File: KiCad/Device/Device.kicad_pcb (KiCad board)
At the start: 2 copper layers, 27 parts, among them IC1 ATTINY167-XUR, J1 Mikrofon, J2 Lysføler, J3 Optisk sensor, J4 Fugtføler, J5 VCC, J6 ESP8266(wifi), SW1 SW_MEC_5E, SW3 SW_MEC_5E, SW4 SW_DIP_x02, Y1 Crystal

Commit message: Fungerende_men_grimt_print
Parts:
- D3: footprint Diode_SMD:D_MELF_Handsoldering -> Resistor_THT:R_Axial_DIN0309_L9.0mm_D3.2mm_P12.70mm_Horizontal
- moved SW3 54.1 mm to (182.2, 61.2)
- moved R6 51.0 mm to (169.3, 93.0), turned to 180 degrees
- moved SW1 46.1 mm to (166.9, 61.1)
- moved D3 44.4 mm to (124.5, 71.1)
- moved C4 43.8 mm to (174.9, 78.0)
- moved D1 40.8 mm to (147.3, 61.0)
- moved J6 39.2 mm to (162.6, 76.2)
- moved D2 36.0 mm to (154.9, 61.0)
- moved C2 35.1 mm to (154.9, 111.8), turned to -90 degrees
- moved R5 34.8 mm to (165.2, 69.0), turned to 180 degrees
- moved Y1 30.9 mm to (162.6, 106.7), turned to -90 degrees
- moved J5 29.7 mm to (121.9, 63.5)
- moved C1 25.4 mm to (195.6, 91.4), turned to -90 degrees
- moved C3 24.3 mm to (170.2, 111.7), turned to -90 degrees
- moved R1 23.2 mm to (132.7, 101.0)
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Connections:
- SW1 pad 2: unconnected-(SW1-Pad2) -> Button01
- SW3 pad 2: unconnected-(SW3-Pad2) -> Reset
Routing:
- net +5V: track 0.00 -> 239.5 mm
- net Reset: track 0.00 -> 134.1 mm, vias 0 -> 4
- net Photo_out: track 0.00 -> 121.2 mm, vias 0 -> 4
- net Net-(C1-Pad1): track 0.00 -> 120.9 mm, vias 0 -> 2
- net Op.Sensor_out: track 0.00 -> 118.6 mm, vias 0 -> 2
- net Fugt_out: track 0.00 -> 105.8 mm
- net Button01: track 0.00 -> 100.3 mm
- net +3,3V: track 0.00 -> 95.5 mm, vias 0 -> 3
- net Net-(D1-Pad1): track 0.00 -> 71.3 mm
- net SCL: track 0.00 -> 50.8 mm, vias 0 -> 2
- net GrønLED: track 0.00 -> 50.3 mm, vias 0 -> 2
- net Net-(D2-Pad1): track 0.00 -> 41.8 mm, vias 0 -> 2
- net SDA: track 0.00 -> 35.3 mm, vias 0 -> 2
- net XTAL1: track 0.00 -> 28.9 mm
- net XTAL2: track 0.00 -> 17.1 mm
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- added copper zone on B.Cu, net GND
- added copper zone on F.Cu, net GND
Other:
- board outline added: 109.6 x 72.2 mm
- board text added: "0 V"
- board text added: "Fugtføler"
- board text added: "Lysføler"
- board text added: "Mic"
- board text added: "Opt. sen."
- board text added: "PAIR"
- board text added: "RESET"
- board text added: "VCC"

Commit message: save
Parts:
- removed J1: Mikrofon, Connector_Phoenix_MC_HighVoltage:PhoenixContact_MCV_1,5_2-G-5.08_1x02_P5.08mm_Vertical
- removed J2: Lysføler, Connector_PinSocket_2.54mm:PinSocket_2x01_P2.54mm_Vertical
- removed J3: Optisk sensor, Connector_PinSocket_2.54mm:PinSocket_2x02_P2.54mm_Vertical
- removed J4: Fugtføler, Connector_PinSocket_2.54mm:PinSocket_1x03_P2.54mm_Vertical
- removed R3: 10k, Resistor_THT:R_Axial_DIN0309_L9.0mm_D3.2mm_P12.70mm_Horizontal
- added J7: Conn_02x06_Counter_Clockwise, Connector_PinHeader_2.54mm:PinHeader_2x06_P2.54mm_Horizontal, F.Cu at (77.1, 35.8)
- added R10: 15, Resistor_THT:R_Axial_DIN0309_L9.0mm_D3.2mm_P12.70mm_Horizontal, F.Cu at (62.8, 69.4)
- C4: footprint Capacitor_THT:C_Disc_D5.0mm_W2.5mm_P5.00mm -> Capacitor_THT:CP_Axial_L10.0mm_D4.5mm_P15.00mm_Horizontal
- D3: footprint Resistor_THT:R_Axial_DIN0309_L9.0mm_D3.2mm_P12.70mm_Horizontal -> Diode_THT:D_DO-15_P10.16mm_Horizontal
- moved C3 138.1 mm to (44.2, 54.9)
- moved C1 133.3 mm to (65.5, 62.1), turned to 0 degrees
- moved IC1 131.7 mm to (60.1, 36.1)
- moved Y1 126.3 mm to (49.6, 50.1)
- moved C2 125.5 mm to (44.4, 52.3), turned to 90 degrees
- moved J6 124.9 mm to (44.2, 36.3)
- moved R6 123.5 mm to (56.6, 42.7), turned to 90 degrees
- moved C4 116.9 mm to (58.9, 63.6), turned to 180 degrees
- moved D1 111.8 mm to (36.3, 74.2), turned to 90 degrees
- moved R5 110.4 mm to (55.2, 59.1), turned to 90 degrees
- moved SW3 107.7 mm to (75.5, 76.1)
- moved SW4 91.7 mm to (46.2, 86.3)
- moved J5 85.8 mm to (38.8, 84.8), turned to 90 degrees
- moved SW1 85.0 mm to (82.0, 61.1), turned to 180 degrees
- moved R4 83.2 mm to (78.5, 29.8), turned to 180 degrees
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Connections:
- net GrønLED renamed LED_G
- net Net-(C1-Pad1) renamed MIC
- C1 pad 2: Mic_out -> UP7
- C4 pad 1: +3,3V -> +3V3
- D3 pad 1: +3,3V -> +3V3
- IC1 pad 11: unconnected-(IC1-Pad11) -> UP7
- IC1 pad 12: unconnected-(IC1-Pad12) -> PHOTRAN
- IC1 pad 13: Op.Sensor_out -> UP5
- IC1 pad 14: Fugt_out -> UP4
- IC1 pad 17: Photo_out -> OPTISK
- IC1 pad 18: Mic_out -> UP2
- IC1 pad 19: unconnected-(IC1-Pad19) -> UP1
- IC1 pad 20: unconnected-(IC1-Pad20) -> DHT11
- J6 pad 4: +3,3V -> +3V3
- J6 pad 8: +3,3V -> +3V3
- R1 pad 1: Photo_out -> PHOTRAN
- R4 pad 1: Op.Sensor_out -> OPTISK
- R9 pad 1: +5V -> +3V3
- R9 pad 2: +3,3V -> +5V
- SW4 pad 2: unconnected-(SW4-Pad2) -> UPWR
- SW4 pad 3: unconnected-(SW4-Pad3) -> +3V3
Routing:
- net Photo_out: track 121.2 -> 0.00 mm, vias 4 -> 0
- net Op.Sensor_out: track 118.6 -> 0.00 mm, vias 2 -> 0
- net MIC: track 120.9 -> 11.6 mm, vias 2 -> 0
- net Fugt_out: track 105.8 -> 0.00 mm
- net +3,3V: track 95.5 -> 0.00 mm, vias 3 -> 0
- net +3V3: track 0.00 -> 75.4 mm
- net Net-(D1-Pad1): track 71.3 -> 4.49 mm
- net Reset: track 134.1 -> 75.2 mm, vias 4 -> 0
- net UP5: track 0.00 -> 57.1 mm
- net UPWR: track 0.00 -> 57.0 mm
- net Button01: track 100.3 -> 53.5 mm
- net OPTISK: track 0.00 -> 45.0 mm
- net +5V: track 239.5 -> 200.4 mm
- net GND: track 0.00 -> 31.7 mm
- net UP7: track 0.00 -> 31.6 mm
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- removed copper zone on B.Cu, net GND
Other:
- board size 109.6 x 72.2 mm -> 53.5 x 62.2 mm
- board text removed: "0 V"
- board text removed: "Fugtføler"
- board text removed: "Lysføler"
- board text removed: "Mic"
- board text removed: "Opt. sen."
- board text removed: "PAIR"
- board text removed: "RESET"
- board text removed: "VCC"

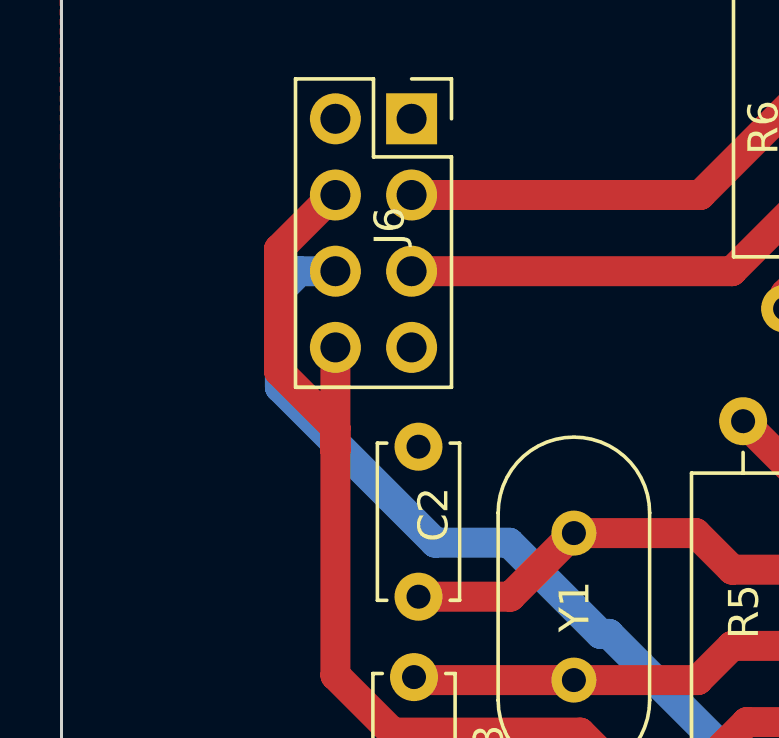
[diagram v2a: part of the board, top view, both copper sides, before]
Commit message: Ny_connecter
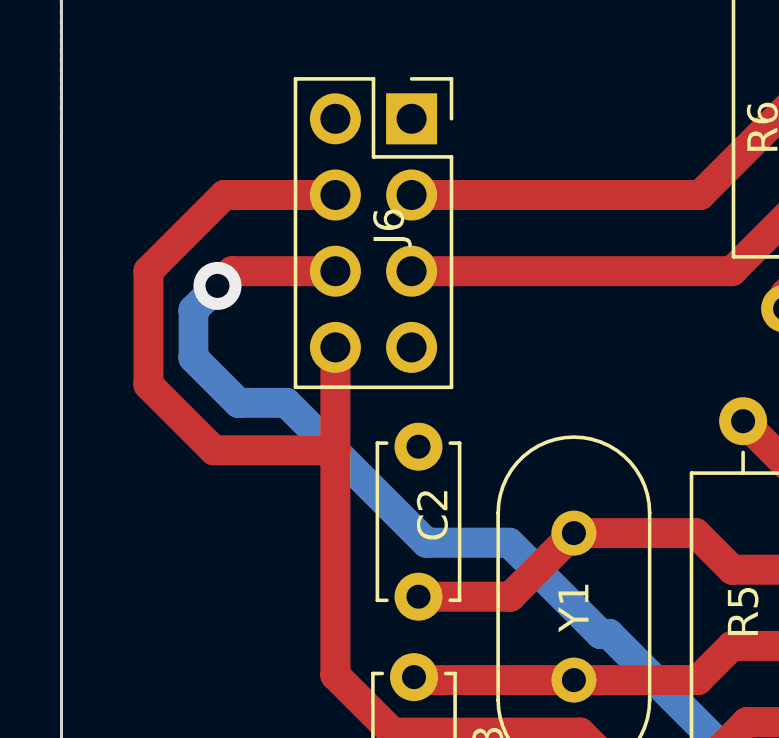
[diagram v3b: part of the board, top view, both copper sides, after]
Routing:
- net +3V3: track 75.4 -> 83.5 mm
- net Reset: track 75.2 -> 80.0 mm, vias 0 -> 1
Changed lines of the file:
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@@
   (segment (start 41.63 54.88) (end 43.539511 56.789511) (width 1) (layer "F.Cu") (net 6))
   (segment (start 49.789511 56.789511) (end 51.410489 58.410489) (width 1) (layer "F.Cu") (net 6))
-  (segment (start 39.75 44.74) (end 39.75 42) (width 1) (layer "F.Cu") (net 6))
+  (segment (start 35.4 45.2) (end 35.4 41.4) (width 1) (layer "F.Cu") (net 6))
   (segment (start 58.86 69.48) (end 58.91 69.43) (width 1) (layer "F.Cu") (net 6))
-  (segment (start 41.554395 38.87) (end 39.75 40.674395) (width 1) (layer "F.Cu") (net 6))
   (segment (start 51.410489 77.910489) (end 52.175 78.675) (width 1) (layer "F.Cu") (net 6))
+  (segment (start 41.63 47.38) (end 37.58 47.38) (width 1) (layer "F.Cu") (net 6))
   (segment (start 41.63 43.95) (end 41.63 47.38) (width 1) (layer "F.Cu") (net 6))
   (segment (start 54.295 78.675) (end 58.86 74.11) (width 1) (layer "F.Cu") (net 6))
   (segment (start 52.175 78.675) (end 54.295 78.675) (width 1) (layer "F.Cu") (net 6))
+  (segment (start 37.58 47.38) (end 35.4 45.2) (width 1) (layer "F.Cu") (net 6))
   (segment (start 48.74 78.675) (end 52.175 78.675) (width 1) (layer "F.Cu") (net 6))
-  (segment (start 41.63 38.87) (end 41.554395 38.87) (width 1) (layer "F.Cu") (net 6))
+  (segment (start 35.4 41.4) (end 37.93 38.87) (width 1) (layer "F.Cu") (net 6))
   (segment (start 58.86 64.445) (end 58.91 64.395) (width 1) (layer "F.Cu") (net 6))
-  (segment (start 39.75 44.74) (end 41.63 46.62) (width 1) (layer "F.Cu") (net 6))
   (segment (start 41.63 47.38) (end 41.63 54.88) (width 1) (layer "F.Cu") (net 6))
-  (segment (start 41.63 46.62) (end 41.63 47.38) (width 1) (layer "F.Cu") (net 6))
-  (segment (start 39.75 40.674395) (end 39.75 42) (width 1) (layer "F.Cu") (net 6))
   (segment (start 51.410489 58.410489) (end 51.410489 77.910489) (width 1) (layer "F.Cu") (net 6))
   (segment (start 43.539511 56.789511) (end 49.789511 56.789511) (width 1) (layer "F.Cu") (net 6))
+  (segment (start 37.93 38.87) (end 41.63 38.87) (width 1) (layer "F.Cu") (net 6))
   (segment (start 58.86 73.5) (end 58.86 64.445) (width 1) (layer "F.Cu") (net 6))
   (segment (start 58.86 74.11) (end 58.86 72.75) (width 1) (layer "F.Cu") (net 6))
@@
   (segment (start 53.21 76.63) (end 53.21 58.575106) (width 1) (layer "F.Cu") (net 14))
   (segment (start 55.345106 56.44) (end 60.14 56.44) (width 1) (layer "F.Cu") (net 14))
+  (segment (start 38.19 41.41) (end 41.63 41.41) (width 1) (layer "F.Cu") (net 15))
   (segment (start 55.22 59.11) (end 60.01 59.11) (width 1) (layer "F.Cu") (net 15))
   (segment (start 60.01 59.11) (end 60.14 58.98) (width 1) (layer "F.Cu") (net 15))
+  (segment (start 37.7 41.9) (end 38.19 41.41) (width 1) (layer "F.Cu") (net 15))
+  (via (at 37.7 41.9) (size 1.6) (drill 0.8) (layers "F.Cu" "B.Cu") (net 15))
+  (segment (start 50.75 53.5) (end 55.22 57.97) (width 1) (layer "B.Cu") (net 15))
   (segment (start 75.54 80.62) (end 82.04 80.62) (width 1) (layer "B.Cu") (net 15))
   (segment (start 55.22 71.654894) (end 64.185106 80.62) (width 1) (layer "B.Cu") (net 15))
+  (segment (start 50.465817 53.5) (end 50.75 53.5) (width 1) (layer "B.Cu") (net 15))
   (segment (start 55.22 57.97) (end 55.22 59.11) (width 1) (layer "B.Cu") (net 15))
-  (segment (start 50.465817 53.5) (end 50.75 53.5) (width 1) (layer "B.Cu") (net 15))
-  (segment (start 50.75 53.5) (end 55.22 57.97) (width 1) (layer "B.Cu") (net 15))
-  (segment (start 39.780489 42.05743) (end 39.780489 45.280489) (width 1) (layer "B.Cu") (net 15))
   (segment (start 64.185106 80.62) (end 75.54 80.62) (width 1) (layer "B.Cu") (net 15))
   (segment (start 47.426306 50.460489) (end 50.465817 53.5) (width 1) (layer "B.Cu") (net 15))
-  (segment (start 39.780489 45.280489) (end 44.960489 50.460489) (width 1) (layer "B.Cu") (net 15))
-  (segment (start 41.63 41.41) (end 40.427919 41.41) (width 1) (layer "B.Cu") (net 15))
-  (segment (start 40.427919 41.41) (end 39.780489 42.05743) (width 1) (layer "B.Cu") (net 15))
-  (segment (start 44.960489 50.460489) (end 47.426306 50.460489) (width 1) (layer "B.Cu") (net 15))
+  (segment (start 38.4 45.8) (end 36.9 44.3) (width 1) (layer "B.Cu") (net 15))
+  (segment (start 44.660489 50.460489) (end 47.426306 50.460489) (width 1) (layer "B.Cu") (net 15))
+  (segment (start 36.9 44.3) (end 36.9 42.7) (width 1) (layer "B.Cu") (net 15))
+  (segment (start 40 45.8) (end 38.4 45.8) (width 1) (layer "B.Cu") (net 15))
+  (segment (start 44.660489 50.460489) (end 40 45.8) (width 1) (layer "B.Cu") (net 15))
+  (segment (start 37.7 41.9) (end 36.9 42.7) (width 1) (layer "B.Cu") (net 15))
   (segment (start 55.22 59.11) (end 55.22 71.654894) (width 1) (layer "B.Cu") (net 15))
   (segment (start 75.937919 45.98) (end 74.34 47.577919) (width 1) (layer "F.Cu") (net 16))

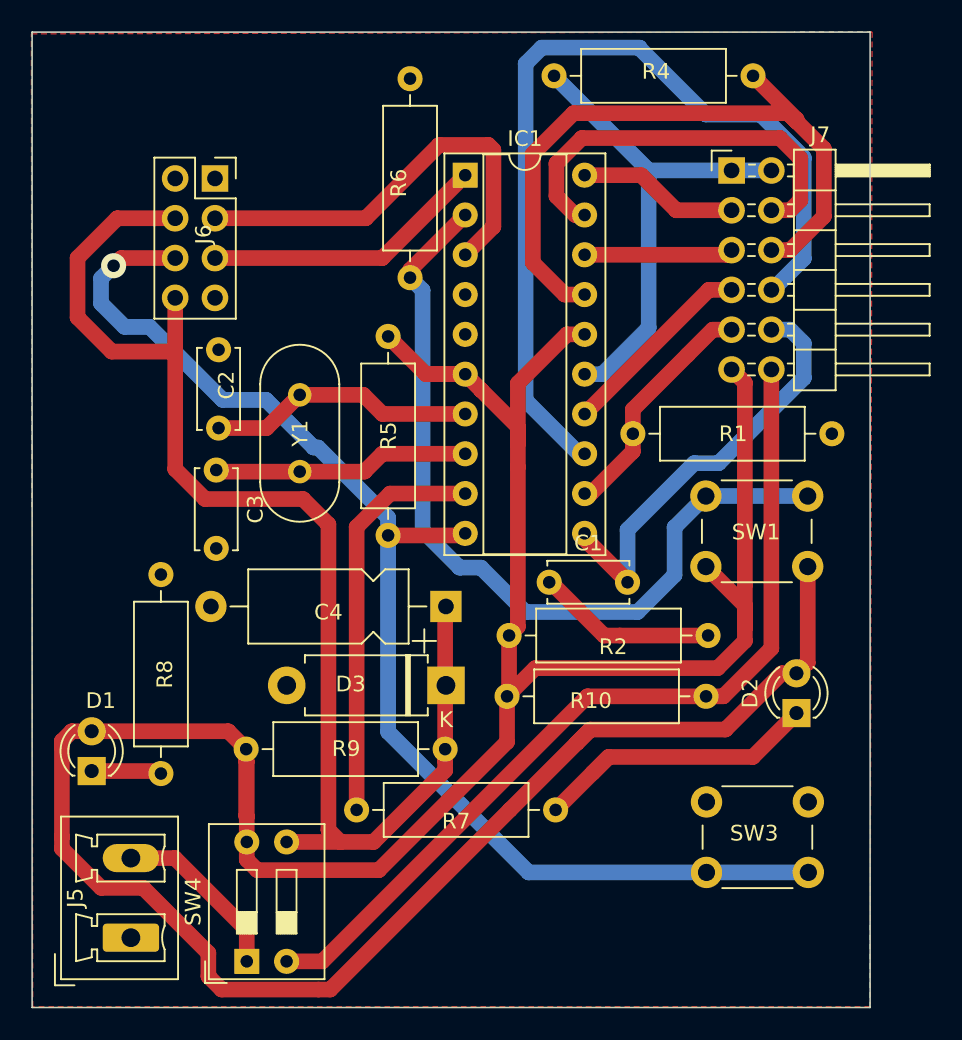
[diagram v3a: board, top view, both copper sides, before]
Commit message: flip sides
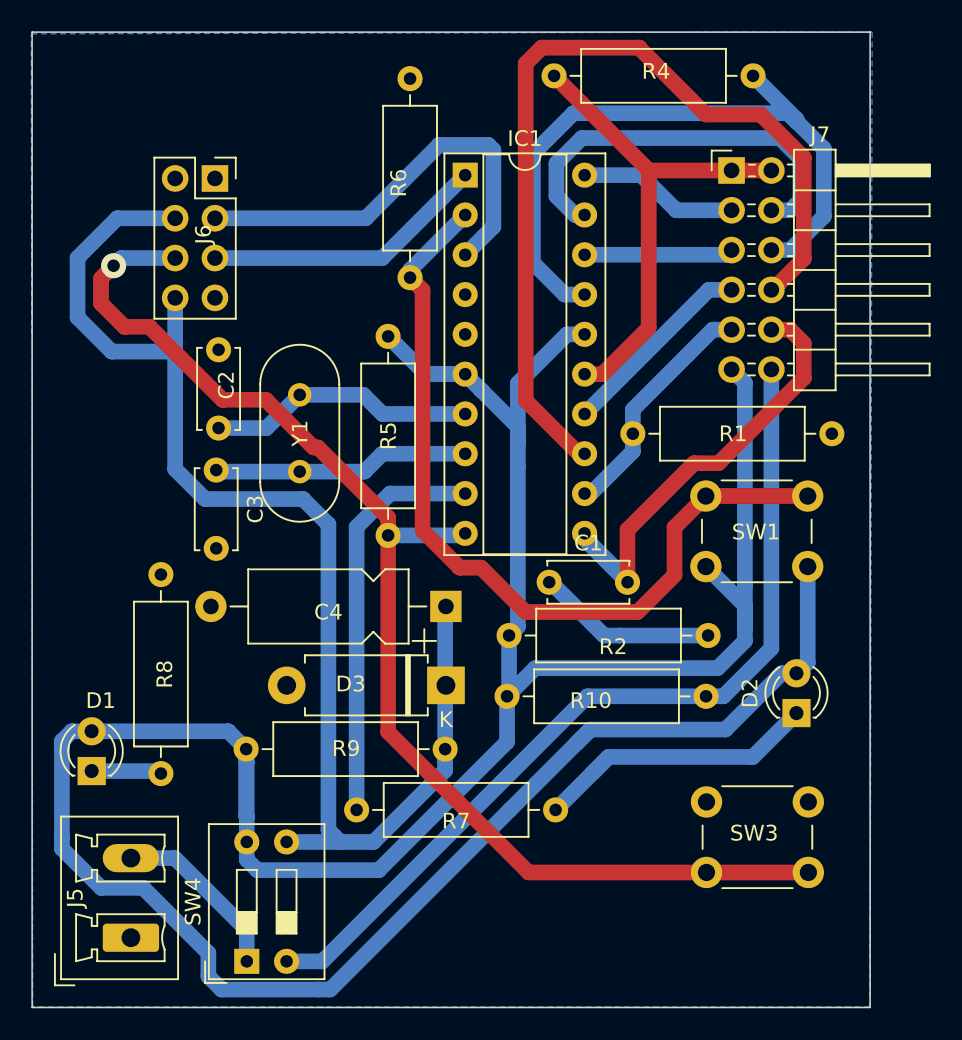
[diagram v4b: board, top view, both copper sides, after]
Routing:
- added copper zone on B.Cu, net GND
- removed copper zone on F.Cu, net GND

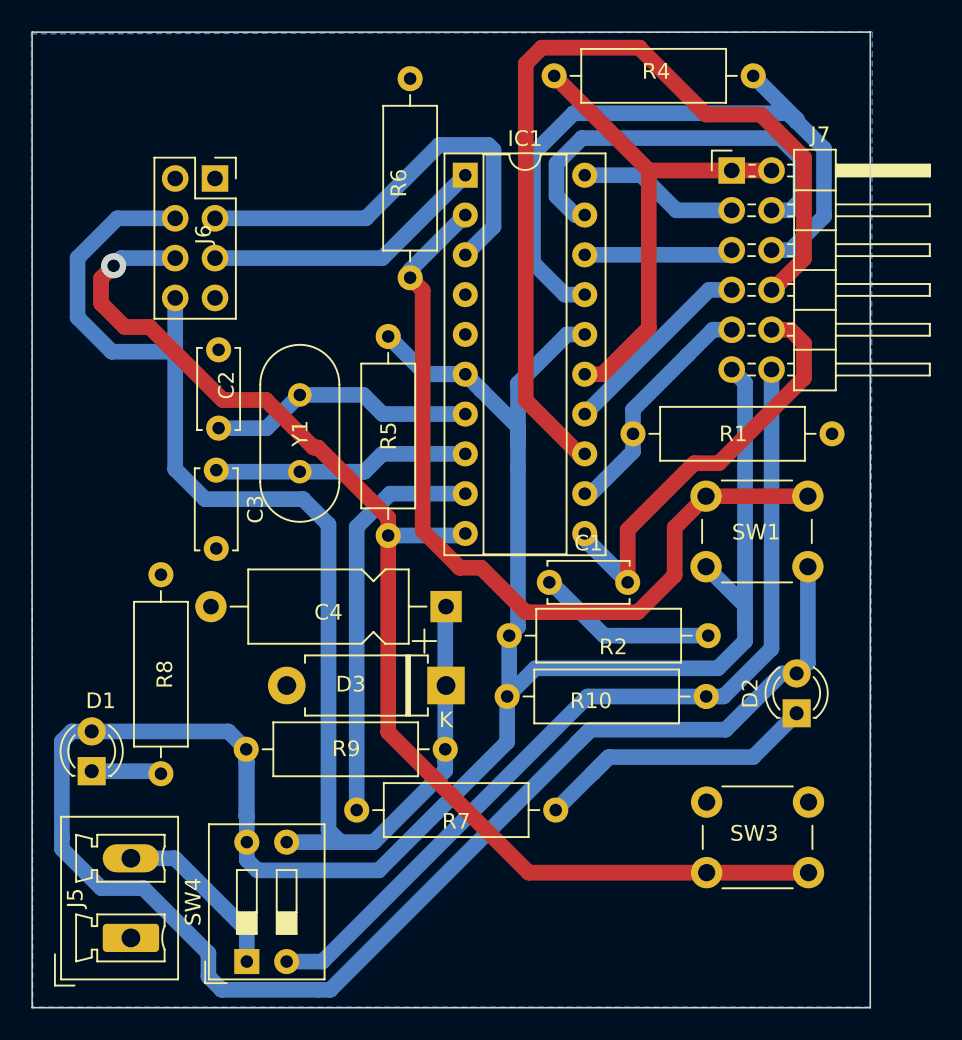
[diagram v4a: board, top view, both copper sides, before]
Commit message: Opdatering af device kicad
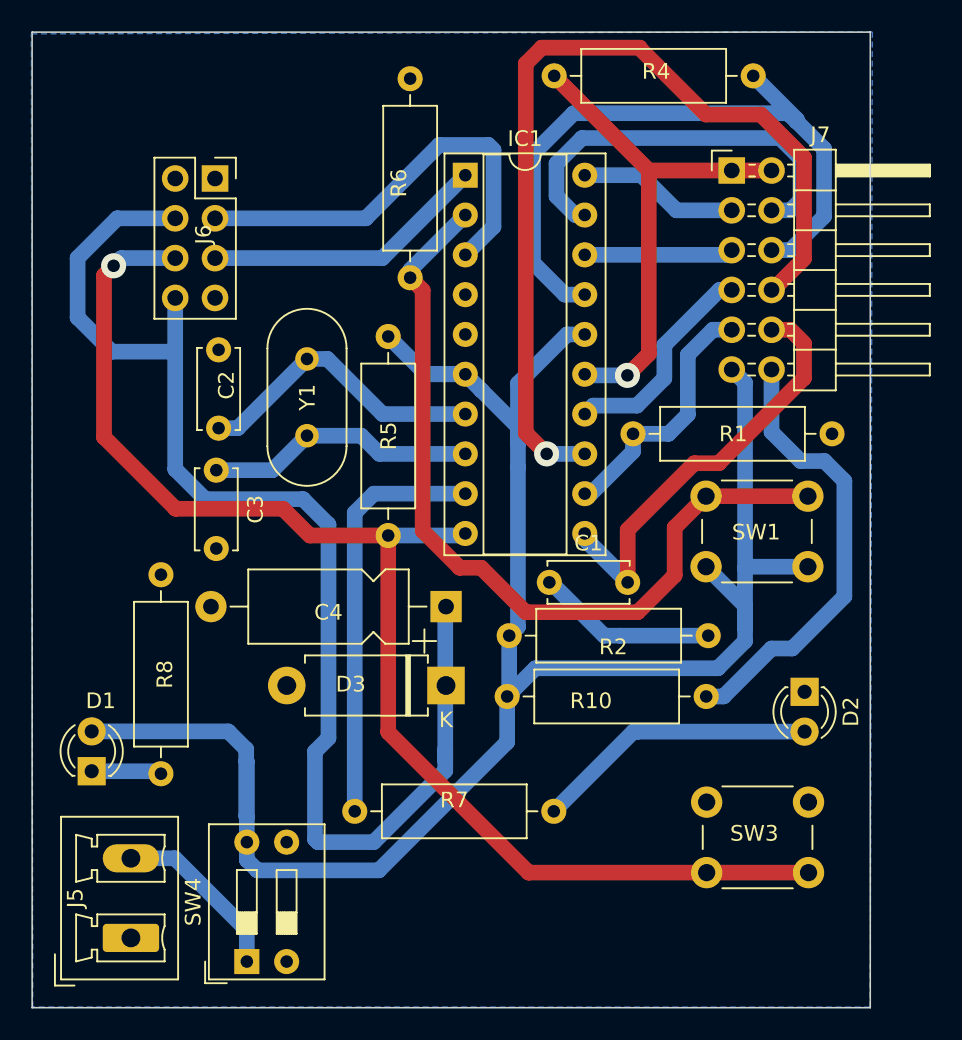
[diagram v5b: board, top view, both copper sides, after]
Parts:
- removed R9: 15, Resistor_THT:R_Axial_DIN0309_L9.0mm_D3.2mm_P12.70mm_Horizontal
- moved R7 12.8 mm to (53.1, 76.7), turned to 0 degrees
- moved Y1 2.34 mm to (50.0, 47.8)
- moved D2 1.46 mm to (81.8, 69.1), turned to -90 degrees
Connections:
- D2 pad 1: Net-(D2-Pad1) -> GND
- D2 pad 2: +5V -> Net-(R7-Pad2)
- R7 pad 1: Net-(D2-Pad1) -> LED_G
- R7 pad 2: LED_G -> Net-(R7-Pad2)
- SW4 pad 2: UPWR -> unconnected-(SW4-Pad2)
- SW4 pad 3: +3V3 -> unconnected-(SW4-Pad3)
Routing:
- net +5V: track 200.4 -> 127.5 mm
- net UPWR: track 57.0 -> 28.8 mm
- net Net-(D2-Pad1): track 19.3 -> 0.00 mm
- net Net-(R7-Pad2): track 0.00 -> 18.1 mm
- net Reset: track 80.0 -> 84.1 mm
- net XTAL1: track 17.1 -> 19.0 mm
- net +3V3: track 83.5 -> 81.7 mm
- net PHOTRAN: track 15.3 -> 16.6 mm
- net UP4: track 12.7 -> 13.9 mm
- net UP5: track 57.1 -> 58.3 mm, vias 0 -> 1
- net GND: track 31.7 -> 32.9 mm, vias 0 -> 1
- net XTAL2: track 16.4 -> 17.4 mm
- net LED_G: track 25.9 -> 26.6 mm

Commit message: Opdateret pcb
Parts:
- added R11: 4.7k, Resistor_THT:R_Axial_DIN0309_L9.0mm_D3.2mm_P12.70mm_Horizontal, F.Cu at (49.3, 32.5)
- added R12: 4.7k, Resistor_THT:R_Axial_DIN0309_L9.0mm_D3.2mm_P12.70mm_Horizontal, F.Cu at (49.3, 28.2)
- moved R10 2.82 mm to (65.0, 71.1)
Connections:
- R10 pad 1: +5V -> +3V3
- R10 pad 2: UPWR -> +5V
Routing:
- net UPWR: track 28.8 -> 0.00 mm
- net +3V3: track 81.7 -> 99.8 mm, vias 0 -> 1
- net SCL: track 27.3 -> 40.9 mm
- net SDA: track 18.2 -> 27.4 mm, vias 0 -> 1
- net +5V: track 127.5 -> 132.3 mm
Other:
- board size 53.5 x 62.2 mm -> 53.5 x 64 mm
